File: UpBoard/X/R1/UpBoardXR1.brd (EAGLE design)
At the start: 88.9 x 76.2 mm, 75 parts, among them CN1 100nF, CN2 100nF, CN3 100nF, CN4 100nF, IC1 SAM3X8E(ARDUINO), IC2 W25N01GVZEIG/IT, Q1 FFB2222A, Q2 FFB2222A, X1 16POS_RIBBON, X2 16POS_RIBBON, X3 16POS_RIBBON, X4 16POS_RIBBON, Y1 FH1200001, Y2 ABS05

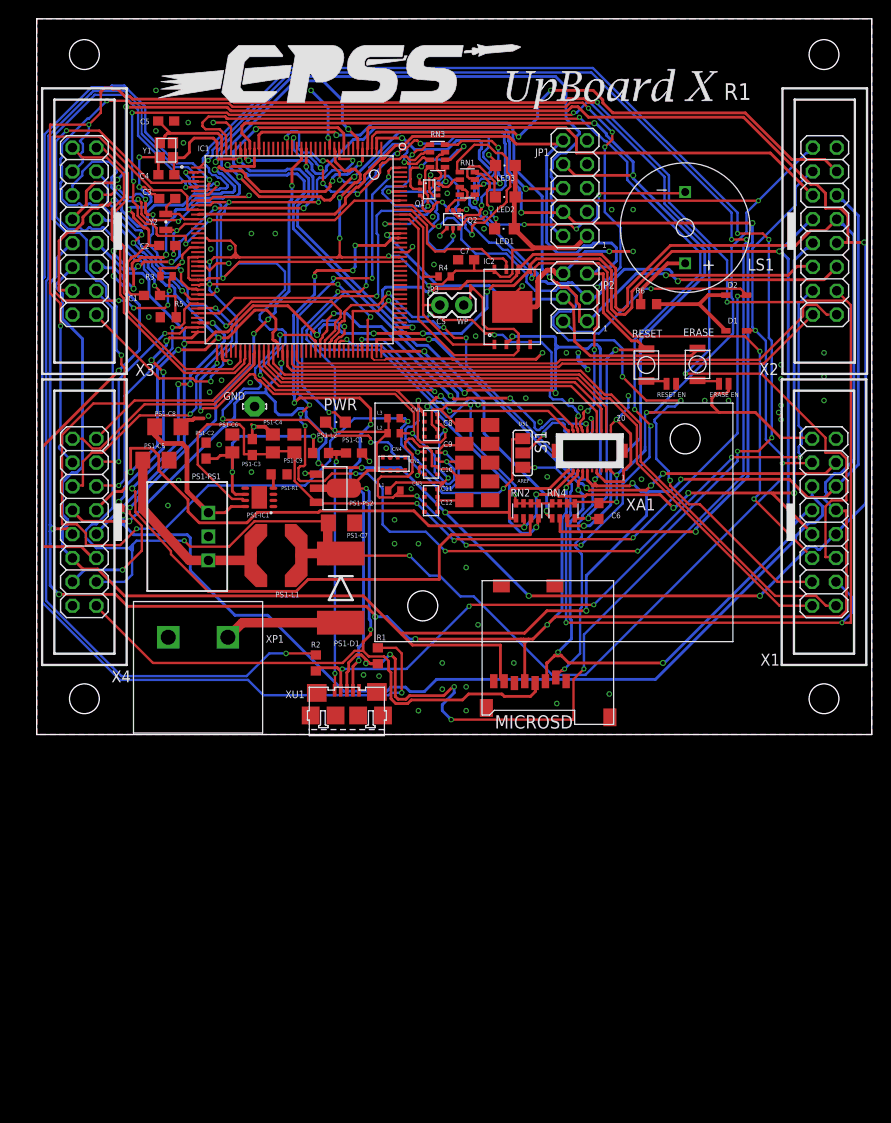
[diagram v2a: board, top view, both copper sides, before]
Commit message: Changed transistors
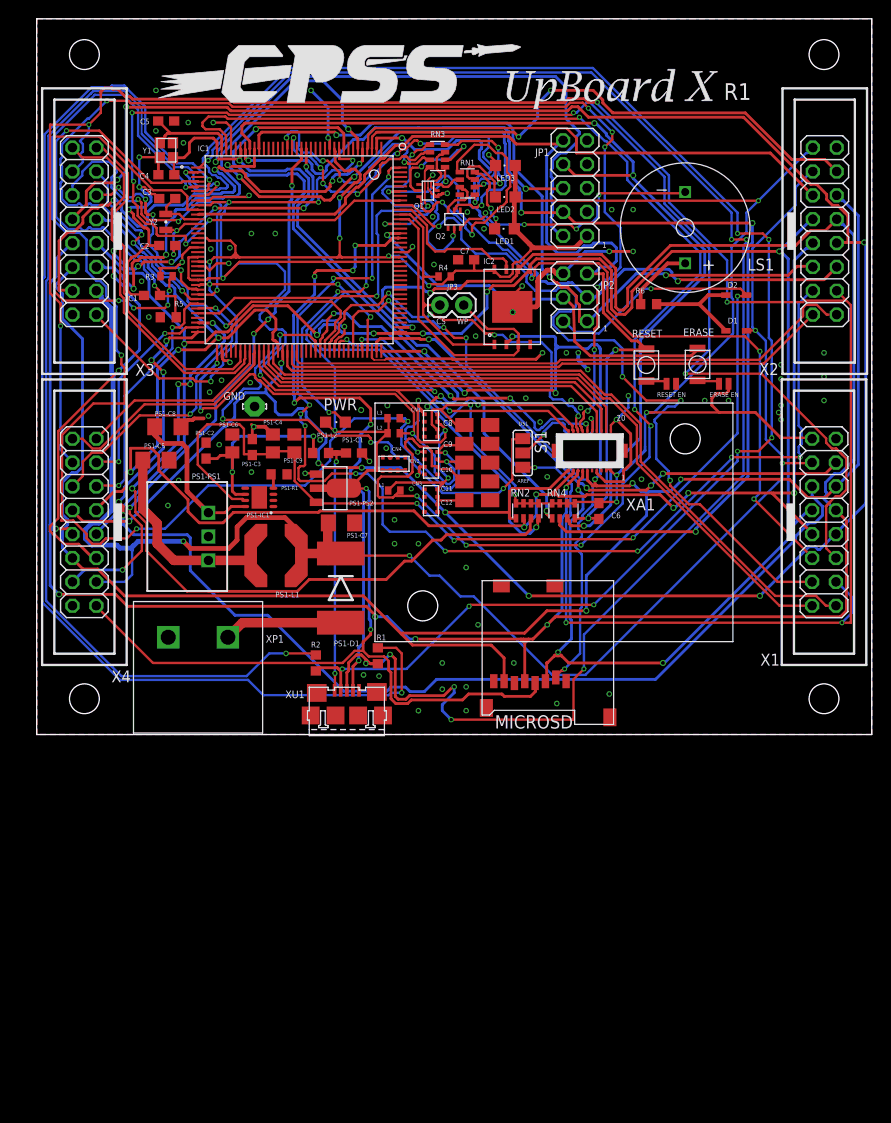
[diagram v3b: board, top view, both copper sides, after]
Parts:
- Q1, Q2: value FFB2222A -> MBT3904DW2T1; device CPSS_IC:SC-88 -> CPSS_IC:SOT-363
- moved Q1 0.18 mm to (41.7, 57.9)
- moved Q2 0.13 mm to (44.5, 54.9)
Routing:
- net D8: track 38.7 -> 33.4 mm
- net TXS3: track 75.0 -> 73.0 mm
- net HV: track 176.2 -> 178.1 mm
- net GND: track 144.4 -> 142.8 mm, vias 87 -> 89
- net D4: track 163.3 -> 162.1 mm
- net PS1-1:N$2: track 19.5 -> 20.6 mm
- net N$19: track 18.8 -> 17.9 mm
- net VDDUTMI: track 138.8 -> 138.1 mm
- net SCK: track 266.7 -> 266.0 mm
- net SCL: track 264.2 -> 263.6 mm
- net D41: track 33.0 -> 32.4 mm
- net MISO: track 242.0 -> 241.5 mm
